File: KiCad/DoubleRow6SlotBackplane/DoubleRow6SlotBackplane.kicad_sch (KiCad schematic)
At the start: 23 parts, among them J0 Conn_02x20_Row_Letter_First, J1 Conn_02x20_Row_Letter_First, J10 Conn_02x20_Row_Letter_First, J11 Conn_02x20_Row_Letter_First, J12 Conn_02x20_Row_Letter_First, J13 Conn_02x20_Row_Letter_First, J14 Conn_02x20_Row_Letter_First, J15 Conn_02x20_Row_Letter_First, J2 Conn_02x20_Row_Letter_First, J3 Conn_02x20_Row_Letter_First, J4 Conn_02x20_Row_Letter_First, J5 Conn_02x20_Row_Letter_First, J6 Conn_02x20_Row_Letter_First, J7 Conn_02x20_Row_Letter_First, J8 Conn_02x20_Row_Letter_First, J9 Conn_02x20_Row_Letter_First

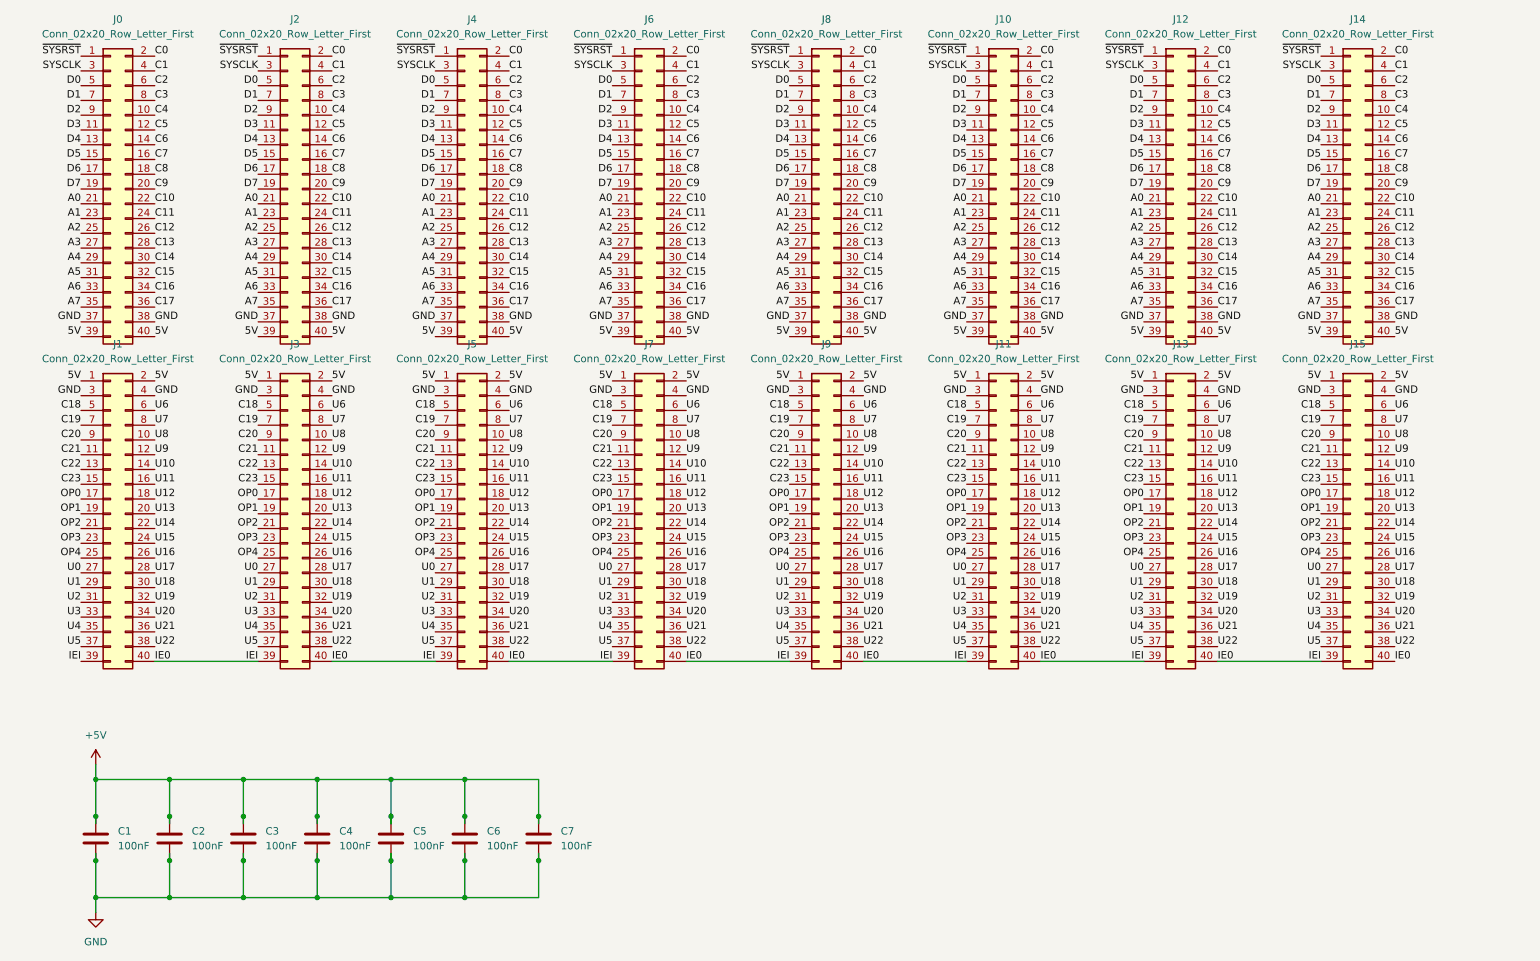
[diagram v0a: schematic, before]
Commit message: Adding 6 slot backplane files
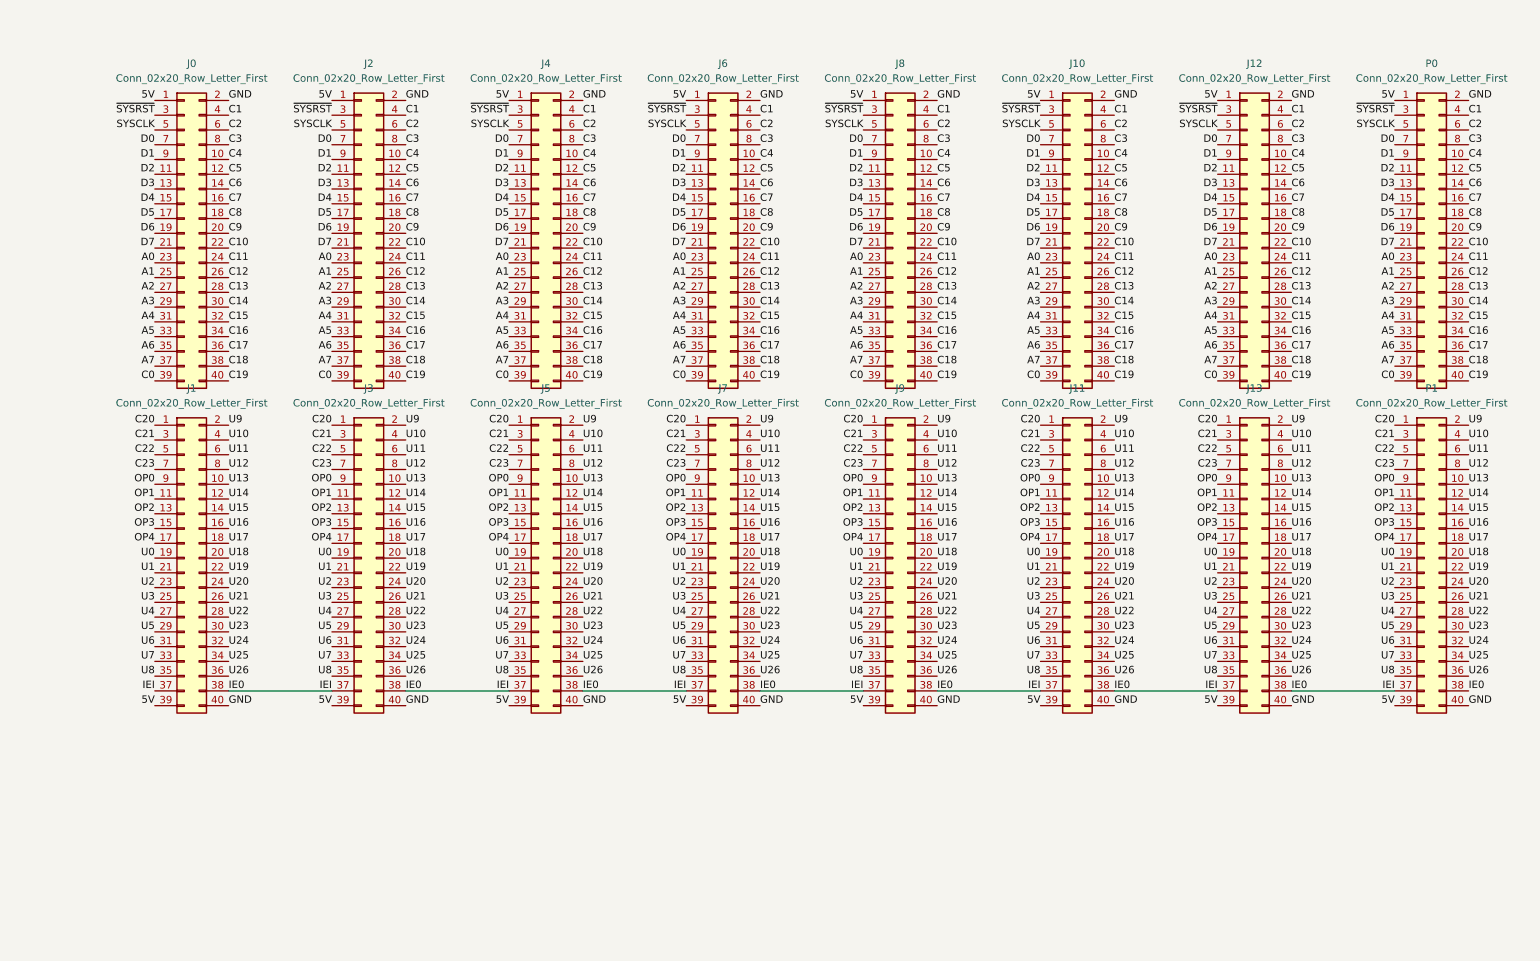
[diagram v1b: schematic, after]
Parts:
- removed C1, C2, C3, C4, C5, C6, C7: 100nF, symbol Device:C
- removed J14, J15: Conn_02x20_Row_Letter_First, Connector_PinHeader_2.54mm:PinHeader_2x20_P2.54mm_Horizontal, symbol Connector_Generic:Conn_02x20_Odd_Even
- added P0, P1: Conn_02x20_Row_Letter_First, Connector_PinHeader_2.54mm:PinHeader_2x20_P2.54mm_Horizontal, symbol Connector_Generic:Conn_02x20_Odd_Even
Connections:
- net 5V: now also J0.1 (Pin_1), J1.39 (Pin_39), J10.1 (Pin_1), J11.39 (Pin_39), J12.1 (Pin_1), J13.39 (Pin_39), J2.1 (Pin_1), J3.39 (Pin_39), J4.1 (Pin_1), J5.39 (Pin_39), J6.1 (Pin_1), J7.39 (Pin_39), J8.1 (Pin_1), J9.39 (Pin_39), P0.1 (Pin_1), P1.39 (Pin_39); no longer J0.39 (Pin_39), J0.40 (Pin_40), J1.1 (Pin_1), J1.2 (Pin_2), J10.39 (Pin_39), J10.40 (Pin_40), J11.1 (Pin_1), J11.2 (Pin_2), J12.39 (Pin_39), J12.40 (Pin_40), J13.1 (Pin_1), J13.2 (Pin_2), J2.39 (Pin_39), J2.40 (Pin_40), J3.1 (Pin_1), J3.2 (Pin_2), J4.39 (Pin_39), J4.40 (Pin_40), J5.1 (Pin_1), J5.2 (Pin_2), J6.39 (Pin_39), J6.40 (Pin_40), J7.1 (Pin_1), J7.2 (Pin_2), J8.39 (Pin_39), J8.40 (Pin_40), J9.1 (Pin_1), J9.2 (Pin_2)
- net A0: now also J0.23 (Pin_23), J10.23 (Pin_23), J12.23 (Pin_23), J2.23 (Pin_23), J4.23 (Pin_23), J6.23 (Pin_23), J8.23 (Pin_23), P0.23 (Pin_23); no longer J0.21 (Pin_21), J10.21 (Pin_21), J12.21 (Pin_21), J2.21 (Pin_21), J4.21 (Pin_21), J6.21 (Pin_21), J8.21 (Pin_21)
- net A1: now also J0.25 (Pin_25), J10.25 (Pin_25), J12.25 (Pin_25), J2.25 (Pin_25), J4.25 (Pin_25), J6.25 (Pin_25), J8.25 (Pin_25), P0.25 (Pin_25); no longer J0.23 (Pin_23), J10.23 (Pin_23), J12.23 (Pin_23), J2.23 (Pin_23), J4.23 (Pin_23), J6.23 (Pin_23), J8.23 (Pin_23)
- net A2: now also J0.27 (Pin_27), J10.27 (Pin_27), J12.27 (Pin_27), J2.27 (Pin_27), J4.27 (Pin_27), J6.27 (Pin_27), J8.27 (Pin_27), P0.27 (Pin_27); no longer J0.25 (Pin_25), J10.25 (Pin_25), J12.25 (Pin_25), J2.25 (Pin_25), J4.25 (Pin_25), J6.25 (Pin_25), J8.25 (Pin_25)
- net A3: now also J0.29 (Pin_29), J10.29 (Pin_29), J12.29 (Pin_29), J2.29 (Pin_29), J4.29 (Pin_29), J6.29 (Pin_29), J8.29 (Pin_29), P0.29 (Pin_29); no longer J0.27 (Pin_27), J10.27 (Pin_27), J12.27 (Pin_27), J2.27 (Pin_27), J4.27 (Pin_27), J6.27 (Pin_27), J8.27 (Pin_27)
- net A4: now also J0.31 (Pin_31), J10.31 (Pin_31), J12.31 (Pin_31), J2.31 (Pin_31), J4.31 (Pin_31), J6.31 (Pin_31), J8.31 (Pin_31), P0.31 (Pin_31); no longer J0.29 (Pin_29), J10.29 (Pin_29), J12.29 (Pin_29), J2.29 (Pin_29), J4.29 (Pin_29), J6.29 (Pin_29), J8.29 (Pin_29)
- net A5: now also J0.33 (Pin_33), J10.33 (Pin_33), J12.33 (Pin_33), J2.33 (Pin_33), J4.33 (Pin_33), J6.33 (Pin_33), J8.33 (Pin_33), P0.33 (Pin_33); no longer J0.31 (Pin_31), J10.31 (Pin_31), J12.31 (Pin_31), J2.31 (Pin_31), J4.31 (Pin_31), J6.31 (Pin_31), J8.31 (Pin_31)
- net A6: now also J0.35 (Pin_35), J10.35 (Pin_35), J12.35 (Pin_35), J2.35 (Pin_35), J4.35 (Pin_35), J6.35 (Pin_35), J8.35 (Pin_35), P0.35 (Pin_35); no longer J0.33 (Pin_33), J10.33 (Pin_33), J12.33 (Pin_33), J2.33 (Pin_33), J4.33 (Pin_33), J6.33 (Pin_33), J8.33 (Pin_33)
- net A7: now also J0.37 (Pin_37), J10.37 (Pin_37), J12.37 (Pin_37), J2.37 (Pin_37), J4.37 (Pin_37), J6.37 (Pin_37), J8.37 (Pin_37), P0.37 (Pin_37); no longer J0.35 (Pin_35), J10.35 (Pin_35), J12.35 (Pin_35), J2.35 (Pin_35), J4.35 (Pin_35), J6.35 (Pin_35), J8.35 (Pin_35)
- net C0: now also J0.39 (Pin_39), J10.39 (Pin_39), J12.39 (Pin_39), J2.39 (Pin_39), J4.39 (Pin_39), J6.39 (Pin_39), J8.39 (Pin_39), P0.39 (Pin_39); no longer J0.2 (Pin_2), J10.2 (Pin_2), J12.2 (Pin_2), J2.2 (Pin_2), J4.2 (Pin_2), J6.2 (Pin_2), J8.2 (Pin_2)
- net C1: now also P0.4 (Pin_4)
- net C10: now also P0.22 (Pin_22)
- net C11: now also P0.24 (Pin_24)
- net C12: now also P0.26 (Pin_26)
- net C13: now also P0.28 (Pin_28)
- net C14: now also P0.30 (Pin_30)
- net C15: now also P0.32 (Pin_32)
- net C16: now also P0.34 (Pin_34)
- net C17: now also P0.36 (Pin_36)
- net C18: now also J0.38 (Pin_38), J10.38 (Pin_38), J12.38 (Pin_38), J2.38 (Pin_38), J4.38 (Pin_38), J6.38 (Pin_38), J8.38 (Pin_38), P0.38 (Pin_38); no longer J1.5 (Pin_5), J11.5 (Pin_5), J13.5 (Pin_5), J3.5 (Pin_5), J5.5 (Pin_5), J7.5 (Pin_5), J9.5 (Pin_5)
- net C19: now also J0.40 (Pin_40), J10.40 (Pin_40), J12.40 (Pin_40), J2.40 (Pin_40), J4.40 (Pin_40), J6.40 (Pin_40), J8.40 (Pin_40), P0.40 (Pin_40); no longer J1.7 (Pin_7), J11.7 (Pin_7), J13.7 (Pin_7), J3.7 (Pin_7), J5.7 (Pin_7), J7.7 (Pin_7), J9.7 (Pin_7)
- net C2: now also P0.6 (Pin_6)
- net C20: now also J1.1 (Pin_1), J11.1 (Pin_1), J13.1 (Pin_1), J3.1 (Pin_1), J5.1 (Pin_1), J7.1 (Pin_1), J9.1 (Pin_1), P1.1 (Pin_1); no longer J1.9 (Pin_9), J11.9 (Pin_9), J13.9 (Pin_9), J3.9 (Pin_9), J5.9 (Pin_9), J7.9 (Pin_9), J9.9 (Pin_9)
- net C21: now also J1.3 (Pin_3), J11.3 (Pin_3), J13.3 (Pin_3), J3.3 (Pin_3), J5.3 (Pin_3), J7.3 (Pin_3), J9.3 (Pin_3), P1.3 (Pin_3); no longer J1.11 (Pin_11), J11.11 (Pin_11), J13.11 (Pin_11), J3.11 (Pin_11), J5.11 (Pin_11), J7.11 (Pin_11), J9.11 (Pin_11)
- net C22: now also J1.5 (Pin_5), J11.5 (Pin_5), J13.5 (Pin_5), J3.5 (Pin_5), J5.5 (Pin_5), J7.5 (Pin_5), J9.5 (Pin_5), P1.5 (Pin_5); no longer J1.13 (Pin_13), J11.13 (Pin_13), J13.13 (Pin_13), J3.13 (Pin_13), J5.13 (Pin_13), J7.13 (Pin_13), J9.13 (Pin_13)
- net C23: now also J1.7 (Pin_7), J11.7 (Pin_7), J13.7 (Pin_7), J3.7 (Pin_7), J5.7 (Pin_7), J7.7 (Pin_7), J9.7 (Pin_7), P1.7 (Pin_7); no longer J1.15 (Pin_15), J11.15 (Pin_15), J13.15 (Pin_15), J3.15 (Pin_15), J5.15 (Pin_15), J7.15 (Pin_15), J9.15 (Pin_15)
- net C3: now also P0.8 (Pin_8)
- net C4: now also P0.10 (Pin_10)
- net C5: now also P0.12 (Pin_12)
- net C6: now also P0.14 (Pin_14)
- net C7: now also P0.16 (Pin_16)
- net C8: now also P0.18 (Pin_18)
- net C9: now also P0.20 (Pin_20)
- net D0: now also J0.7 (Pin_7), J10.7 (Pin_7), J12.7 (Pin_7), J2.7 (Pin_7), J4.7 (Pin_7), J6.7 (Pin_7), J8.7 (Pin_7), P0.7 (Pin_7); no longer J0.5 (Pin_5), J10.5 (Pin_5), J12.5 (Pin_5), J2.5 (Pin_5), J4.5 (Pin_5), J6.5 (Pin_5), J8.5 (Pin_5)
- net D1: now also J0.9 (Pin_9), J10.9 (Pin_9), J12.9 (Pin_9), J2.9 (Pin_9), J4.9 (Pin_9), J6.9 (Pin_9), J8.9 (Pin_9), P0.9 (Pin_9); no longer J0.7 (Pin_7), J10.7 (Pin_7), J12.7 (Pin_7), J2.7 (Pin_7), J4.7 (Pin_7), J6.7 (Pin_7), J8.7 (Pin_7)
- net D2: now also J0.11 (Pin_11), J10.11 (Pin_11), J12.11 (Pin_11), J2.11 (Pin_11), J4.11 (Pin_11), J6.11 (Pin_11), J8.11 (Pin_11), P0.11 (Pin_11); no longer J0.9 (Pin_9), J10.9 (Pin_9), J12.9 (Pin_9), J2.9 (Pin_9), J4.9 (Pin_9), J6.9 (Pin_9), J8.9 (Pin_9)
- net D3: now also J0.13 (Pin_13), J10.13 (Pin_13), J12.13 (Pin_13), J2.13 (Pin_13), J4.13 (Pin_13), J6.13 (Pin_13), J8.13 (Pin_13), P0.13 (Pin_13); no longer J0.11 (Pin_11), J10.11 (Pin_11), J12.11 (Pin_11), J2.11 (Pin_11), J4.11 (Pin_11), J6.11 (Pin_11), J8.11 (Pin_11)
- net D4: now also J0.15 (Pin_15), J10.15 (Pin_15), J12.15 (Pin_15), J2.15 (Pin_15), J4.15 (Pin_15), J6.15 (Pin_15), J8.15 (Pin_15), P0.15 (Pin_15); no longer J0.13 (Pin_13), J10.13 (Pin_13), J12.13 (Pin_13), J2.13 (Pin_13), J4.13 (Pin_13), J6.13 (Pin_13), J8.13 (Pin_13)
- net D5: now also J0.17 (Pin_17), J10.17 (Pin_17), J12.17 (Pin_17), J2.17 (Pin_17), J4.17 (Pin_17), J6.17 (Pin_17), J8.17 (Pin_17), P0.17 (Pin_17); no longer J0.15 (Pin_15), J10.15 (Pin_15), J12.15 (Pin_15), J2.15 (Pin_15), J4.15 (Pin_15), J6.15 (Pin_15), J8.15 (Pin_15)
- net D6: now also J0.19 (Pin_19), J10.19 (Pin_19), J12.19 (Pin_19), J2.19 (Pin_19), J4.19 (Pin_19), J6.19 (Pin_19), J8.19 (Pin_19), P0.19 (Pin_19); no longer J0.17 (Pin_17), J10.17 (Pin_17), J12.17 (Pin_17), J2.17 (Pin_17), J4.17 (Pin_17), J6.17 (Pin_17), J8.17 (Pin_17)
- net D7: now also J0.21 (Pin_21), J10.21 (Pin_21), J12.21 (Pin_21), J2.21 (Pin_21), J4.21 (Pin_21), J6.21 (Pin_21), J8.21 (Pin_21), P0.21 (Pin_21); no longer J0.19 (Pin_19), J10.19 (Pin_19), J12.19 (Pin_19), J2.19 (Pin_19), J4.19 (Pin_19), J6.19 (Pin_19), J8.19 (Pin_19)
- net GND: now also J0.2 (Pin_2), J1.40 (Pin_40), J10.2 (Pin_2), J11.40 (Pin_40), J12.2 (Pin_2), J13.40 (Pin_40), J2.2 (Pin_2), J3.40 (Pin_40), J4.2 (Pin_2), J5.40 (Pin_40), J6.2 (Pin_2), J7.40 (Pin_40), J8.2 (Pin_2), J9.40 (Pin_40), P0.2 (Pin_2), P1.40 (Pin_40); no longer J0.37 (Pin_37), J0.38 (Pin_38), J1.3 (Pin_3), J1.4 (Pin_4), J10.37 (Pin_37), J10.38 (Pin_38), J11.3 (Pin_3), J11.4 (Pin_4), J12.37 (Pin_37), J12.38 (Pin_38), J13.3 (Pin_3), J13.4 (Pin_4), J2.37 (Pin_37), J2.38 (Pin_38), J3.3 (Pin_3), J3.4 (Pin_4), J4.37 (Pin_37), J4.38 (Pin_38), J5.3 (Pin_3), J5.4 (Pin_4), J6.37 (Pin_37), J6.38 (Pin_38), J7.3 (Pin_3), J7.4 (Pin_4), J8.37 (Pin_37), J8.38 (Pin_38), J9.3 (Pin_3), J9.4 (Pin_4)
- net IE0: now also J1.37 (Pin_37), J1.38 (Pin_38), J11.37 (Pin_37), J11.38 (Pin_38), J13.37 (Pin_37), J13.38 (Pin_38), J3.37 (Pin_37), J3.38 (Pin_38), J5.37 (Pin_37), J5.38 (Pin_38), J7.37 (Pin_37), J7.38 (Pin_38), J9.37 (Pin_37), J9.38 (Pin_38), P1.37 (Pin_37), P1.38 (Pin_38); no longer J1.39 (Pin_39), J1.40 (Pin_40), J11.39 (Pin_39), J11.40 (Pin_40), J13.39 (Pin_39), J13.40 (Pin_40), J3.39 (Pin_39), J3.40 (Pin_40), J5.39 (Pin_39), J5.40 (Pin_40), J7.39 (Pin_39), J7.40 (Pin_40), J9.39 (Pin_39), J9.40 (Pin_40)
- net OP0: now also J1.9 (Pin_9), J11.9 (Pin_9), J13.9 (Pin_9), J3.9 (Pin_9), J5.9 (Pin_9), J7.9 (Pin_9), J9.9 (Pin_9), P1.9 (Pin_9); no longer J1.17 (Pin_17), J11.17 (Pin_17), J13.17 (Pin_17), J3.17 (Pin_17), J5.17 (Pin_17), J7.17 (Pin_17), J9.17 (Pin_17)
- net OP1: now also J1.11 (Pin_11), J11.11 (Pin_11), J13.11 (Pin_11), J3.11 (Pin_11), J5.11 (Pin_11), J7.11 (Pin_11), J9.11 (Pin_11), P1.11 (Pin_11); no longer J1.19 (Pin_19), J11.19 (Pin_19), J13.19 (Pin_19), J3.19 (Pin_19), J5.19 (Pin_19), J7.19 (Pin_19), J9.19 (Pin_19)
- net OP2: now also J1.13 (Pin_13), J11.13 (Pin_13), J13.13 (Pin_13), J3.13 (Pin_13), J5.13 (Pin_13), J7.13 (Pin_13), J9.13 (Pin_13), P1.13 (Pin_13); no longer J1.21 (Pin_21), J11.21 (Pin_21), J13.21 (Pin_21), J3.21 (Pin_21), J5.21 (Pin_21), J7.21 (Pin_21), J9.21 (Pin_21)
- net OP3: now also J1.15 (Pin_15), J11.15 (Pin_15), J13.15 (Pin_15), J3.15 (Pin_15), J5.15 (Pin_15), J7.15 (Pin_15), J9.15 (Pin_15), P1.15 (Pin_15); no longer J1.23 (Pin_23), J11.23 (Pin_23), J13.23 (Pin_23), J3.23 (Pin_23), J5.23 (Pin_23), J7.23 (Pin_23), J9.23 (Pin_23)
- net OP4: now also J1.17 (Pin_17), J11.17 (Pin_17), J13.17 (Pin_17), J3.17 (Pin_17), J5.17 (Pin_17), J7.17 (Pin_17), J9.17 (Pin_17), P1.17 (Pin_17); no longer J1.25 (Pin_25), J11.25 (Pin_25), J13.25 (Pin_25), J3.25 (Pin_25), J5.25 (Pin_25), J7.25 (Pin_25), J9.25 (Pin_25)
- net SYSCLK: now also J0.5 (Pin_5), J10.5 (Pin_5), J12.5 (Pin_5), J2.5 (Pin_5), J4.5 (Pin_5), J6.5 (Pin_5), J8.5 (Pin_5), P0.5 (Pin_5); no longer J0.3 (Pin_3), J10.3 (Pin_3), J12.3 (Pin_3), J2.3 (Pin_3), J4.3 (Pin_3), J6.3 (Pin_3), J8.3 (Pin_3)
- net U0: now also J1.19 (Pin_19), J11.19 (Pin_19), J13.19 (Pin_19), J3.19 (Pin_19), J5.19 (Pin_19), J7.19 (Pin_19), J9.19 (Pin_19), P1.19 (Pin_19); no longer J1.27 (Pin_27), J11.27 (Pin_27), J13.27 (Pin_27), J3.27 (Pin_27), J5.27 (Pin_27), J7.27 (Pin_27), J9.27 (Pin_27)
- net U1: now also J1.21 (Pin_21), J11.21 (Pin_21), J13.21 (Pin_21), J3.21 (Pin_21), J5.21 (Pin_21), J7.21 (Pin_21), J9.21 (Pin_21), P1.21 (Pin_21); no longer J1.29 (Pin_29), J11.29 (Pin_29), J13.29 (Pin_29), J3.29 (Pin_29), J5.29 (Pin_29), J7.29 (Pin_29), J9.29 (Pin_29)
- net U10: now also J1.4 (Pin_4), J11.4 (Pin_4), J13.4 (Pin_4), J3.4 (Pin_4), J5.4 (Pin_4), J7.4 (Pin_4), J9.4 (Pin_4), P1.4 (Pin_4); no longer J1.14 (Pin_14), J11.14 (Pin_14), J13.14 (Pin_14), J3.14 (Pin_14), J5.14 (Pin_14), J7.14 (Pin_14), J9.14 (Pin_14)
- net U11: now also J1.6 (Pin_6), J11.6 (Pin_6), J13.6 (Pin_6), J3.6 (Pin_6), J5.6 (Pin_6), J7.6 (Pin_6), J9.6 (Pin_6), P1.6 (Pin_6); no longer J1.16 (Pin_16), J11.16 (Pin_16), J13.16 (Pin_16), J3.16 (Pin_16), J5.16 (Pin_16), J7.16 (Pin_16), J9.16 (Pin_16)
- net U12: now also J1.8 (Pin_8), J11.8 (Pin_8), J13.8 (Pin_8), J3.8 (Pin_8), J5.8 (Pin_8), J7.8 (Pin_8), J9.8 (Pin_8), P1.8 (Pin_8); no longer J1.18 (Pin_18), J11.18 (Pin_18), J13.18 (Pin_18), J3.18 (Pin_18), J5.18 (Pin_18), J7.18 (Pin_18), J9.18 (Pin_18)
- net U13: now also J1.10 (Pin_10), J11.10 (Pin_10), J13.10 (Pin_10), J3.10 (Pin_10), J5.10 (Pin_10), J7.10 (Pin_10), J9.10 (Pin_10), P1.10 (Pin_10); no longer J1.20 (Pin_20), J11.20 (Pin_20), J13.20 (Pin_20), J3.20 (Pin_20), J5.20 (Pin_20), J7.20 (Pin_20), J9.20 (Pin_20)
- net U14: now also J1.12 (Pin_12), J11.12 (Pin_12), J13.12 (Pin_12), J3.12 (Pin_12), J5.12 (Pin_12), J7.12 (Pin_12), J9.12 (Pin_12), P1.12 (Pin_12); no longer J1.22 (Pin_22), J11.22 (Pin_22), J13.22 (Pin_22), J3.22 (Pin_22), J5.22 (Pin_22), J7.22 (Pin_22), J9.22 (Pin_22)
- net U15: now also J1.14 (Pin_14), J11.14 (Pin_14), J13.14 (Pin_14), J3.14 (Pin_14), J5.14 (Pin_14), J7.14 (Pin_14), J9.14 (Pin_14), P1.14 (Pin_14); no longer J1.24 (Pin_24), J11.24 (Pin_24), J13.24 (Pin_24), J3.24 (Pin_24), J5.24 (Pin_24), J7.24 (Pin_24), J9.24 (Pin_24)
- net U16: now also J1.16 (Pin_16), J11.16 (Pin_16), J13.16 (Pin_16), J3.16 (Pin_16), J5.16 (Pin_16), J7.16 (Pin_16), J9.16 (Pin_16), P1.16 (Pin_16); no longer J1.26 (Pin_26), J11.26 (Pin_26), J13.26 (Pin_26), J3.26 (Pin_26), J5.26 (Pin_26), J7.26 (Pin_26), J9.26 (Pin_26)
- net U17: now also J1.18 (Pin_18), J11.18 (Pin_18), J13.18 (Pin_18), J3.18 (Pin_18), J5.18 (Pin_18), J7.18 (Pin_18), J9.18 (Pin_18), P1.18 (Pin_18); no longer J1.28 (Pin_28), J11.28 (Pin_28), J13.28 (Pin_28), J3.28 (Pin_28), J5.28 (Pin_28), J7.28 (Pin_28), J9.28 (Pin_28)
- net U18: now also J1.20 (Pin_20), J11.20 (Pin_20), J13.20 (Pin_20), J3.20 (Pin_20), J5.20 (Pin_20), J7.20 (Pin_20), J9.20 (Pin_20), P1.20 (Pin_20); no longer J1.30 (Pin_30), J11.30 (Pin_30), J13.30 (Pin_30), J3.30 (Pin_30), J5.30 (Pin_30), J7.30 (Pin_30), J9.30 (Pin_30)
- net U19: now also J1.22 (Pin_22), J11.22 (Pin_22), J13.22 (Pin_22), J3.22 (Pin_22), J5.22 (Pin_22), J7.22 (Pin_22), J9.22 (Pin_22), P1.22 (Pin_22); no longer J1.32 (Pin_32), J11.32 (Pin_32), J13.32 (Pin_32), J3.32 (Pin_32), J5.32 (Pin_32), J7.32 (Pin_32), J9.32 (Pin_32)
- net U2: now also J1.23 (Pin_23), J11.23 (Pin_23), J13.23 (Pin_23), J3.23 (Pin_23), J5.23 (Pin_23), J7.23 (Pin_23), J9.23 (Pin_23), P1.23 (Pin_23); no longer J1.31 (Pin_31), J11.31 (Pin_31), J13.31 (Pin_31), J3.31 (Pin_31), J5.31 (Pin_31), J7.31 (Pin_31), J9.31 (Pin_31)
- net U20: now also J1.24 (Pin_24), J11.24 (Pin_24), J13.24 (Pin_24), J3.24 (Pin_24), J5.24 (Pin_24), J7.24 (Pin_24), J9.24 (Pin_24), P1.24 (Pin_24); no longer J1.34 (Pin_34), J11.34 (Pin_34), J13.34 (Pin_34), J3.34 (Pin_34), J5.34 (Pin_34), J7.34 (Pin_34), J9.34 (Pin_34)
- net U21: now also J1.26 (Pin_26), J11.26 (Pin_26), J13.26 (Pin_26), J3.26 (Pin_26), J5.26 (Pin_26), J7.26 (Pin_26), J9.26 (Pin_26), P1.26 (Pin_26); no longer J1.36 (Pin_36), J11.36 (Pin_36), J13.36 (Pin_36), J3.36 (Pin_36), J5.36 (Pin_36), J7.36 (Pin_36), J9.36 (Pin_36)
- net U22: now also J1.28 (Pin_28), J11.28 (Pin_28), J13.28 (Pin_28), J3.28 (Pin_28), J5.28 (Pin_28), J7.28 (Pin_28), J9.28 (Pin_28), P1.28 (Pin_28); no longer J1.38 (Pin_38), J11.38 (Pin_38), J13.38 (Pin_38), J3.38 (Pin_38), J5.38 (Pin_38), J7.38 (Pin_38), J9.38 (Pin_38)
- net U3: now also J1.25 (Pin_25), J11.25 (Pin_25), J13.25 (Pin_25), J3.25 (Pin_25), J5.25 (Pin_25), J7.25 (Pin_25), J9.25 (Pin_25), P1.25 (Pin_25); no longer J1.33 (Pin_33), J11.33 (Pin_33), J13.33 (Pin_33), J3.33 (Pin_33), J5.33 (Pin_33), J7.33 (Pin_33), J9.33 (Pin_33)
- net U4: now also J1.27 (Pin_27), J11.27 (Pin_27), J13.27 (Pin_27), J3.27 (Pin_27), J5.27 (Pin_27), J7.27 (Pin_27), J9.27 (Pin_27), P1.27 (Pin_27); no longer J1.35 (Pin_35), J11.35 (Pin_35), J13.35 (Pin_35), J3.35 (Pin_35), J5.35 (Pin_35), J7.35 (Pin_35), J9.35 (Pin_35)
- net U5: now also J1.29 (Pin_29), J11.29 (Pin_29), J13.29 (Pin_29), J3.29 (Pin_29), J5.29 (Pin_29), J7.29 (Pin_29), J9.29 (Pin_29), P1.29 (Pin_29); no longer J1.37 (Pin_37), J11.37 (Pin_37), J13.37 (Pin_37), J3.37 (Pin_37), J5.37 (Pin_37), J7.37 (Pin_37), J9.37 (Pin_37)
- net U6: now also J1.31 (Pin_31), J11.31 (Pin_31), J13.31 (Pin_31), J3.31 (Pin_31), J5.31 (Pin_31), J7.31 (Pin_31), J9.31 (Pin_31), P1.31 (Pin_31); no longer J1.6 (Pin_6), J11.6 (Pin_6), J13.6 (Pin_6), J3.6 (Pin_6), J5.6 (Pin_6), J7.6 (Pin_6), J9.6 (Pin_6)
- net U7: now also J1.33 (Pin_33), J11.33 (Pin_33), J13.33 (Pin_33), J3.33 (Pin_33), J5.33 (Pin_33), J7.33 (Pin_33), J9.33 (Pin_33), P1.33 (Pin_33); no longer J1.8 (Pin_8), J11.8 (Pin_8), J13.8 (Pin_8), J3.8 (Pin_8), J5.8 (Pin_8), J7.8 (Pin_8), J9.8 (Pin_8)
- net U8: now also J1.35 (Pin_35), J11.35 (Pin_35), J13.35 (Pin_35), J3.35 (Pin_35), J5.35 (Pin_35), J7.35 (Pin_35), J9.35 (Pin_35), P1.35 (Pin_35); no longer J1.10 (Pin_10), J11.10 (Pin_10), J13.10 (Pin_10), J3.10 (Pin_10), J5.10 (Pin_10), J7.10 (Pin_10), J9.10 (Pin_10)
- net U9: now also J1.2 (Pin_2), J11.2 (Pin_2), J13.2 (Pin_2), J3.2 (Pin_2), J5.2 (Pin_2), J7.2 (Pin_2), J9.2 (Pin_2), P1.2 (Pin_2); no longer J1.12 (Pin_12), J11.12 (Pin_12), J13.12 (Pin_12), J3.12 (Pin_12), J5.12 (Pin_12), J7.12 (Pin_12), J9.12 (Pin_12)
- net ~{SYSRST}: now also J0.3 (Pin_3), J10.3 (Pin_3), J12.3 (Pin_3), J2.3 (Pin_3), J4.3 (Pin_3), J6.3 (Pin_3), J8.3 (Pin_3), P0.3 (Pin_3); no longer J0.1 (Pin_1), J10.1 (Pin_1), J12.1 (Pin_1), J2.1 (Pin_1), J4.1 (Pin_1), J6.1 (Pin_1), J8.1 (Pin_1)
- new net U23: J1.30 (Pin_30), J11.30 (Pin_30), J13.30 (Pin_30), J3.30 (Pin_30), J5.30 (Pin_30), J7.30 (Pin_30), J9.30 (Pin_30), P1.30 (Pin_30)
- new net U24: J1.32 (Pin_32), J11.32 (Pin_32), J13.32 (Pin_32), J3.32 (Pin_32), J5.32 (Pin_32), J7.32 (Pin_32), J9.32 (Pin_32), P1.32 (Pin_32)
- new net U25: J1.34 (Pin_34), J11.34 (Pin_34), J13.34 (Pin_34), J3.34 (Pin_34), J5.34 (Pin_34), J7.34 (Pin_34), J9.34 (Pin_34), P1.34 (Pin_34)
- new net U26: J1.36 (Pin_36), J11.36 (Pin_36), J13.36 (Pin_36), J3.36 (Pin_36), J5.36 (Pin_36), J7.36 (Pin_36), J9.36 (Pin_36), P1.36 (Pin_36)
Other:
- moved on the sheet: J0, J1
